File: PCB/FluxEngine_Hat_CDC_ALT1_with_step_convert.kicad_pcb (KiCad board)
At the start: 2 copper layers, 83.3 x 24.1 mm, 8 parts, among them J1 CY8CKIT-059, J2 5V, J3 24V, P1 FDC_BUS_IBMPC, P2 FDC_BUS_CDC_alt1, U1 74HC00

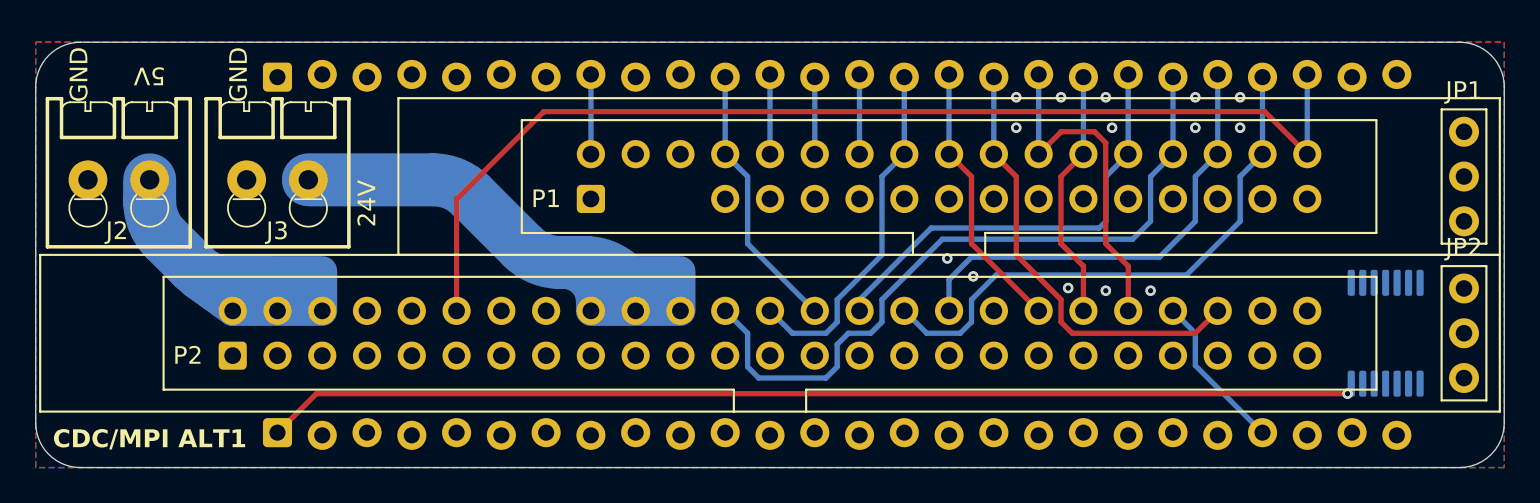
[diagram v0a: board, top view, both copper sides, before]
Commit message: WIP add step convert
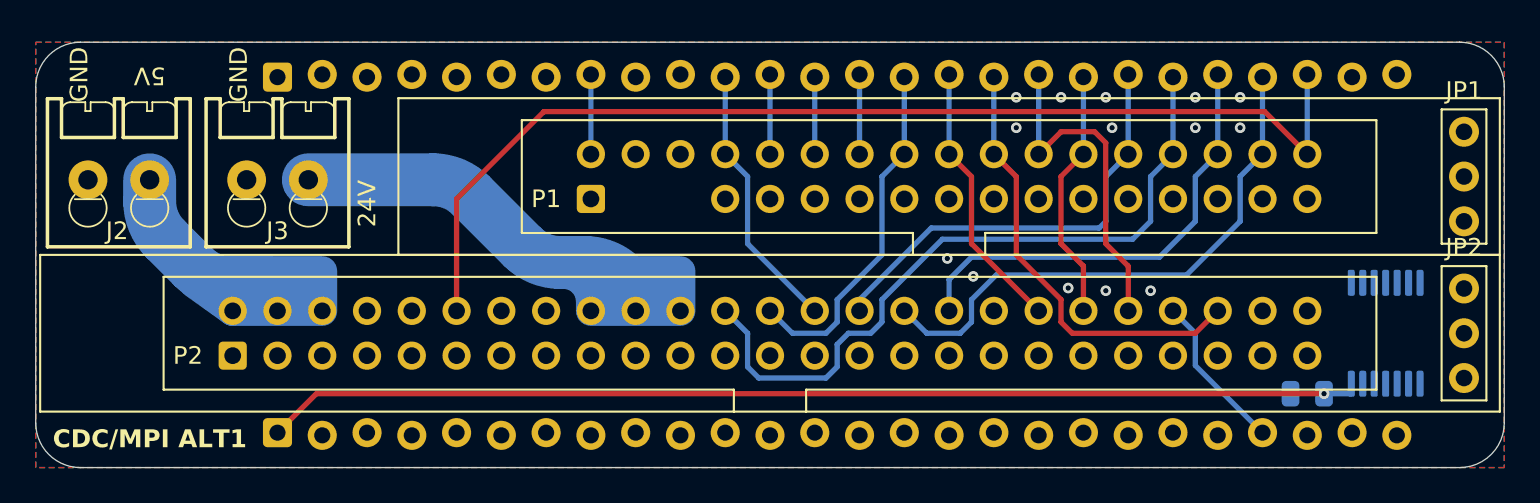
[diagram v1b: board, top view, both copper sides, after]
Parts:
- added C1: 0.1u, Capacitor_SMD:C_0805_2012Metric, B.Cu at (174.6, 104.4)
